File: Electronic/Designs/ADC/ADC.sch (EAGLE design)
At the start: 12 parts

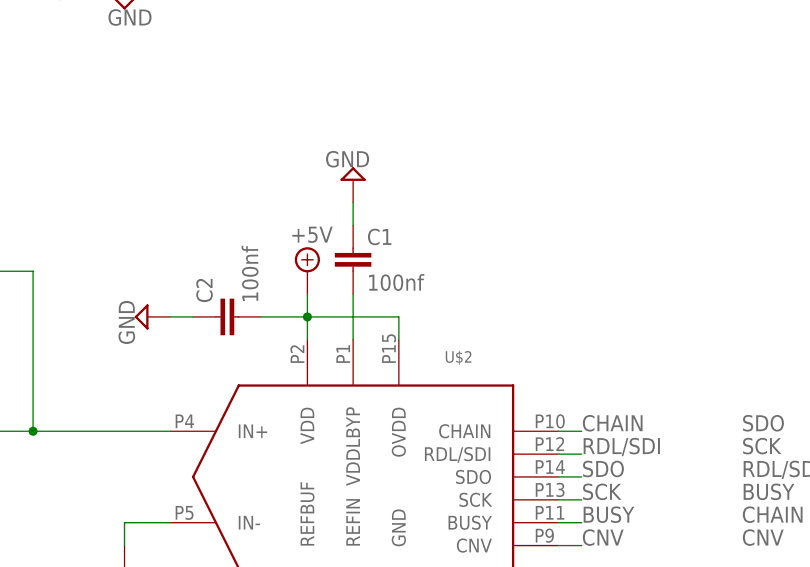
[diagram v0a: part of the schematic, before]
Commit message: moved silkscreen text in ADC
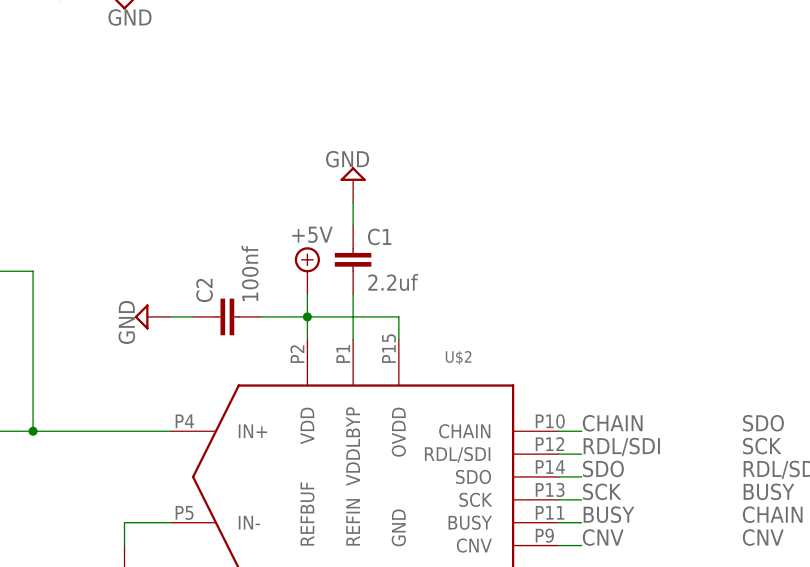
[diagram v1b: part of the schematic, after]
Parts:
- C1: value 100nf -> 2.2uf
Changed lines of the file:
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@@
 <part name="U$2" library="LTC2326-16" deviceset="LTC2326-16" device=""/>
 <part name="SUPPLY1" library="supply2" deviceset="GND" device=""/>
-<part name="C1" library="resistor" deviceset="C-EU" device="C0603" value="100nf"/>
+<part name="C1" library="resistor" deviceset="C-EU" device="C0603" value="2.2uf"/>
 <part name="C2" library="resistor" deviceset="C-EU" device="C0603" value="100nf"/>
 <part name="C3" library="resistor" deviceset="C-EU" device="C0603" value="100nf"/>
